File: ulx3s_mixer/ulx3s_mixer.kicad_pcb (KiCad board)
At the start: 4 copper layers, 66 x 62 mm, 47 parts, among them J1 Conn_02x20_Odd_Even, J2 Conn_Coaxial, Q1 BC846, U1 MAX2606, U2 ADEX-10L+, U3 VAM-6+, U4 PL133-27

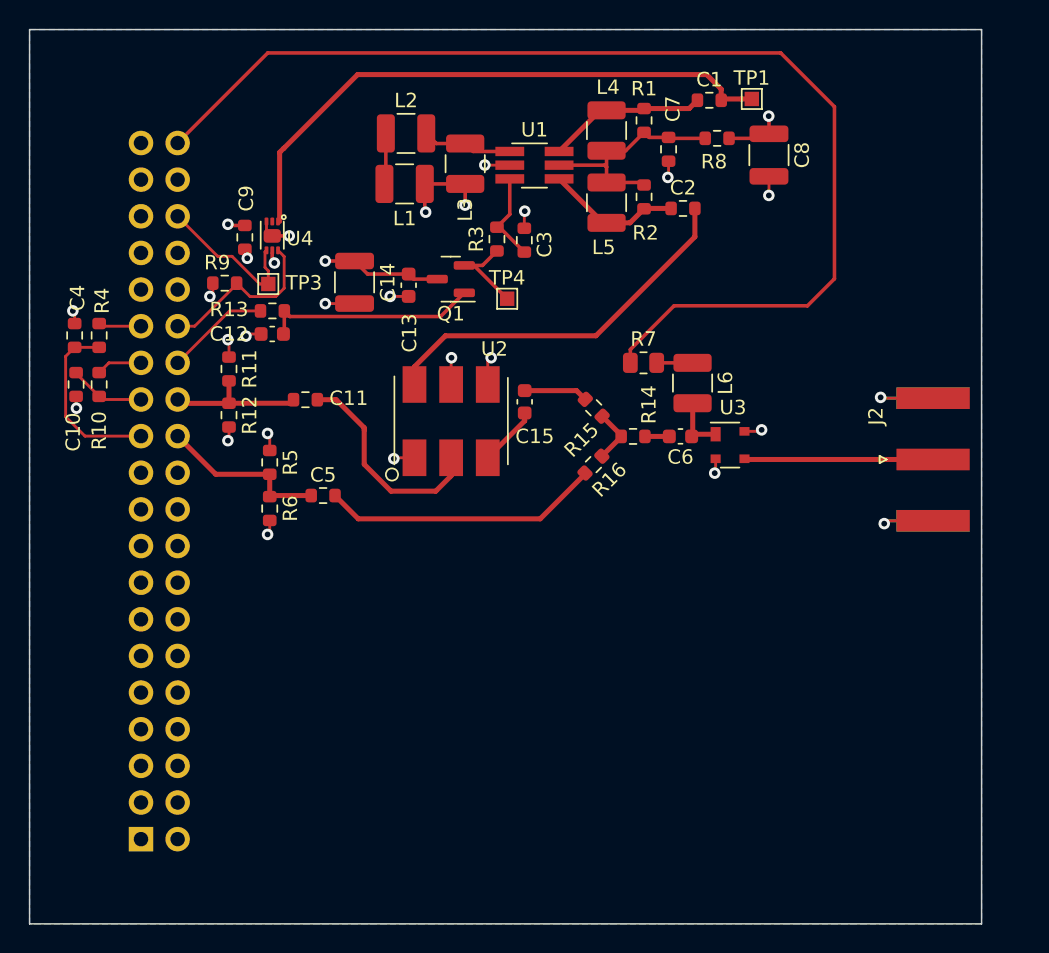
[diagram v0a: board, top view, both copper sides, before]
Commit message: Added design rules and poly pour (zone) on top layer
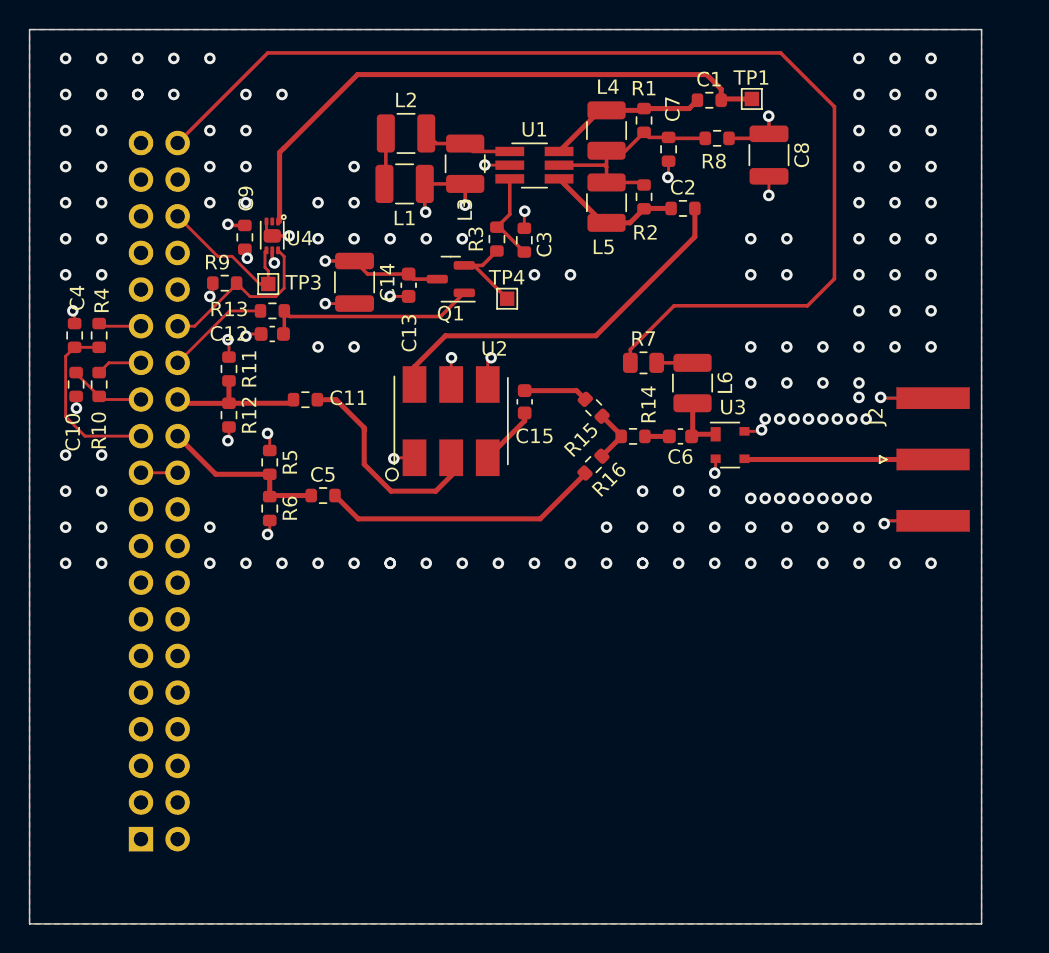
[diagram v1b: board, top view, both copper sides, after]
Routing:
- net GND: track 46.2 -> 48.7 mm, vias 23 -> 162
- added copper zone on F.Cu, net GND

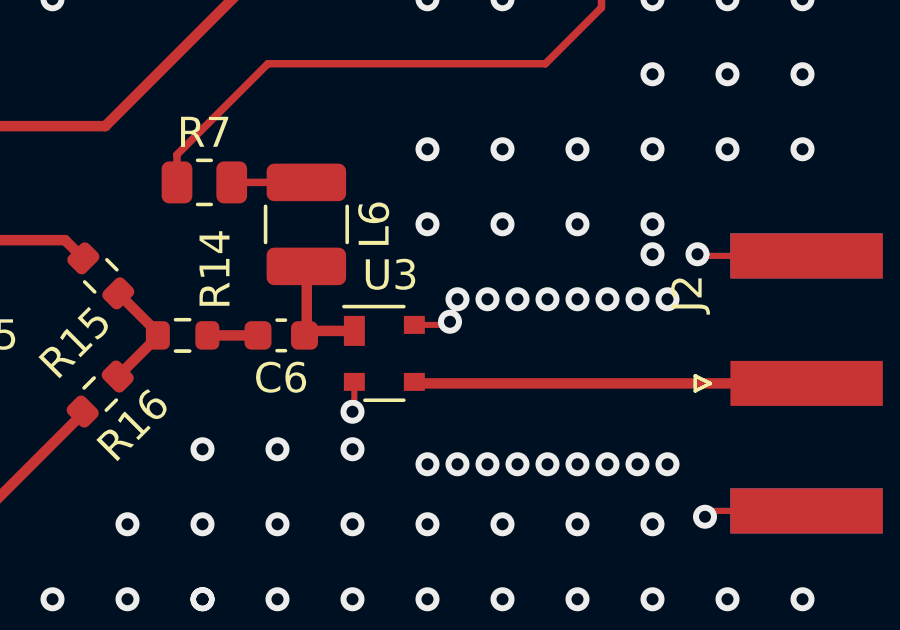
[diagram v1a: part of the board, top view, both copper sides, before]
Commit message: Added start of CS4344
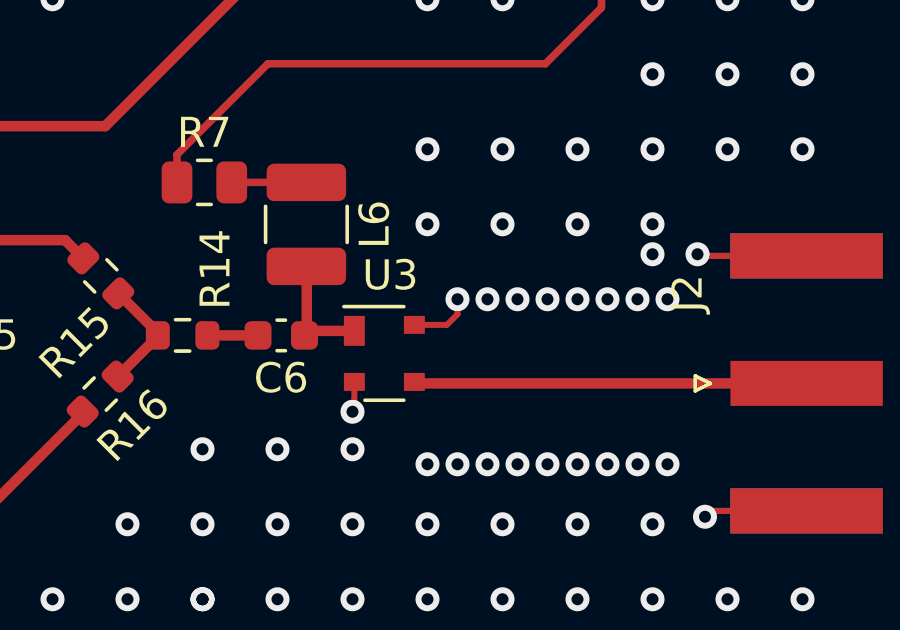
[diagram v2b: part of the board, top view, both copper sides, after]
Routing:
- net GND: track 48.7 -> 49.6 mm, vias 162 -> 161
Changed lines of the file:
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@@
   (segment (start 141.26 59.49) (end 141.25 59.5) (width 0.2) (layer "F.Cu") (net 6))
   (segment (start 116.685 77.685) (end 115.315 77.685) (width 0.2) (layer "F.Cu") (net 6))
-  (segment (start 140.645 75.855) (end 140.75 75.75) (width 0.2) (layer "F.Cu") (net 6))
-  (segment (start 139.5625 75.855) (end 140.645 75.855) (width 0.2) (layer "F.Cu") (net 6))
   (segment (start 134.3 57.125) (end 134.3 58.2) (width 0.2) (layer "F.Cu") (net 6))
   (segment (start 115.315 77.685) (end 115.25 77.75) (width 0.2) (layer "F.Cu") (net 6))
@@
   (segment (start 105.145 69.105) (end 105 69.25) (width 0.2) (layer "F.Cu") (net 6))
   (segment (start 137.5625 77.755) (end 137.5625 78.6875) (width 0.2) (layer "F.Cu") (net 6))
+  (segment (start 140.645 75.855) (end 141 75.5) (width 0.2) (layer "F.Cu") (net 6))
+  (segment (start 141 75.5) (end 141 75) (width 0.2) (layer "F.Cu") (net 6))
   (segment (start 116.28 66.5) (end 115 66.5) (width 0.2) (layer "F.Cu") (net 6))
   (segment (start 93.125 68.38) (end 93.125 67.625) (width 0.2) (layer "F.Cu") (net 6))
@@
   (segment (start 102.705 66.295) (end 102.5 66.5) (width 0.2) (layer "F.Cu") (net 6))
   (segment (start 149.055 73.555) (end 152.6375 73.555) (width 0.2) (layer "F.Cu") (net 6))
+  (segment (start 139.5625 75.855) (end 140.645 75.855) (width 0.2) (layer "F.Cu") (net 6))
   (segment (start 93.225 74.225) (end 93.25 74.25) (width 0.2) (layer "F.Cu") (net 6))
   (via (at 140 72.5) (size 0.8) (drill 0.4) (layers "F.Cu" "B.Cu") (free) (net 6))
@@
   (via (at 93 67.5) (size 0.8) (drill 0.4) (layers "F.Cu" "B.Cu") (net 6))
   (via (at 110 62.5) (size 0.8) (drill 0.4) (layers "F.Cu" "B.Cu") (free) (net 6))
-  (via (at 141 75) (size 0.8) (drill 0.4) (layers "F.Cu" "B.Cu") (free) (net 6))
   (via (at 137.5 80) (size 0.8) (drill 0.4) (layers "F.Cu" "B.Cu") (free) (net 6))
   (via (at 102.5 85) (size 0.8) (drill 0.4) (layers "F.Cu" "B.Cu") (free) (net 6))
@@
   (via (at 130 82.5) (size 0.8) (drill 0.4) (layers "F.Cu" "B.Cu") (free) (net 6))
   (via (at 127.5 65) (size 0.8) (drill 0.4) (layers "F.Cu" "B.Cu") (free) (net 6))
-  (via (at 147.5 82.5) (size 0.8) (drill 0.4) (layers "F.Cu" "B.Cu") (free) (net 6))
   (via (at 145 80.5) (size 0.8) (drill 0.4) (layers "F.Cu" "B.Cu") (free) (net 6))
   (via (at 117.5 62.5) (size 0.8) (drill 0.4) (layers "F.Cu" "B.Cu") (free) (net 6))
@@
   (via (at 110 85) (size 0.8) (drill 0.4) (layers "F.Cu" "B.Cu") (free) (net 6))
   (via (at 110 70) (size 0.8) (drill 0.4) (layers "F.Cu" "B.Cu") (free) (net 6))
-  (via (at 140.75 75.75) (size 0.8) (drill 0.4) (layers "F.Cu" "B.Cu") (net 6))
+  (via (at 141 75) (size 0.8) (drill 0.4) (layers "F.Cu" "B.Cu") (net 6))
   (via (at 122.5 85) (size 0.8) (drill 0.4) (layers "F.Cu" "B.Cu") (free) (net 6))
   (via (at 95 50) (size 0.8) (drill 0.4) (layers "F.Cu" "B.Cu") (free) (net 6))
@@
   (via (at 152.5 85) (size 0.8) (drill 0.4) (layers "F.Cu" "B.Cu") (free) (net 6))
   (via (at 135 80) (size 0.8) (drill 0.4) (layers "F.Cu" "B.Cu") (free) (net 6))
+  (via (at 147.5 82.5) (size 0.8) (drill 0.4) (layers "F.Cu" "B.Cu") (free) (net 6))
   (via (at 97.5 52.5) (size 0.8) (drill 0.4) (layers "F.Cu" "B.Cu") (free) (net 6))
   (via (at 132.5 85) (size 0.8) (drill 0.4) (layers "F.Cu" "B.Cu") (free) (net 6))

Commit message: Finished design, exported BOM + gerbers
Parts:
- added C16: 100nF, Capacitor_SMD:C_0603_1608Metric, F.Cu at (131.0, 96.0)
- added C17: 10uF, Capacitor_SMD:C_1210_3225Metric, F.Cu at (128.0, 94.5)
- added C18: 100nF, Capacitor_SMD:C_0603_1608Metric, F.Cu at (133.5, 94.3)
- added C19: 100nF, Capacitor_SMD:C_0603_1608Metric, F.Cu at (111.5, 95.3)
- added C20: 10uF, Capacitor_SMD:C_1210_3225Metric, F.Cu at (114.0, 95.5)
- added C21: 10uF, Capacitor_SMD:C_1210_3225Metric, F.Cu at (121.0, 97.0)
- added C22: 3.3uF, Capacitor_SMD:C_1210_3225Metric, F.Cu at (131.5, 103.0)
- added C23: 3.3uF, Capacitor_SMD:C_1210_3225Metric, F.Cu at (136.0, 95.0)
- added C24: 2.7nF, Capacitor_SMD:C_0603_1608Metric, F.Cu at (140.0, 96.0)
- added C25: 2.7nF, Capacitor_SMD:C_0603_1608Metric, F.Cu at (139.5, 104.0)
- added FB1: FerriteBead, Inductor_SMD:L_0402_1005Metric, F.Cu at (131.5, 93.5)
- added J3: AudioJack3_Ground, Connector_Audio:Jack_3.5mm_CUI_SJ-3523-SMT_Horizontal, F.Cu at (150.0, 98.5)
- added R17: 1R, Resistor_SMD:R_0603_1608Metric, F.Cu at (128.0, 98.5)
- added R18: 10k, Resistor_SMD:R_0603_1608Metric, F.Cu at (134.5, 103.0)
- added R19: 10k, Resistor_SMD:R_0603_1608Metric, F.Cu at (135.7, 90.5)
- added R20: 470R, Resistor_SMD:R_0603_1608Metric, F.Cu at (138.5, 101.5)
- added R21: 470R, Resistor_SMD:R_0603_1608Metric, F.Cu at (139.3, 93.5)
- added U5: CS4344, Package_SO:TSSOP-10_3x3mm_P0.5mm, F.Cu at (119.0, 92.5)
- R7: value 92R -> 100R
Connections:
- J1 pad 12: unconnected-(J1-Pad12) -> /MCLK
- J1 pad 14: unconnected-(J1-Pad14) -> /LRCLK
- J1 pad 16: unconnected-(J1-Pad16) -> /SCLK
- J1 pad 18: unconnected-(J1-Pad18) -> /SDIN
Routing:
- net +3V3: track 16.2 -> 56.0 mm
- net Net-(C22-Pad1): track 0.00 -> 23.9 mm
- net Net-(C23-Pad1): track 0.00 -> 21.5 mm
- net /SDIN: track 0.00 -> 19.8 mm
- net /SCLK: track 0.00 -> 18.9 mm
- net /LRCLK: track 0.00 -> 18.1 mm
- net /MCLK: track 0.00 -> 17.2 mm
- net Net-(C25-Pad2): track 0.00 -> 14.3 mm
- net +3.3VA: track 0.00 -> 12.2 mm
- net Net-(C22-Pad2): track 0.00 -> 6.72 mm
- net Net-(C24-Pad2): track 0.00 -> 6.16 mm
- net Net-(C19-Pad1): track 0.00 -> 5.76 mm
- net Net-(C23-Pad2): track 0.00 -> 5.04 mm
- net GND: track 49.6 -> 54.0 mm, vias 161 -> 273
- net Net-(C21-Pad1): track 0.00 -> 2.18 mm
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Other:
- board text added: "0"
- board text added: "0 mm"
- board text added: "0.01 mm"
- board text added: "0.0175 mm"
- board text added: "0.02"
- board text added: "0.035 mm"
- board text added: "0.196 mm"
- board text added: "1"
- board text added: "1.03 mm"
- board text added: "3.3"
- board text added: "4.5"
- board text added: "B.Cu"
- board text added: "B.Mask"
- board text added: "B.Paste"
- board text added: "B.Silkscreen"
- board text added: "Bottom Silk Screen"
- board text added: "Bottom Solder Mask"
- board text added: "Bottom Solder Paste"
- board text added: "Color"
- board text added: "Dielectric"
- board text added: "Epsilon R"
- board text added: "F.Cu"
- board text added: "F.Mask"
- board text added: "F.Paste"
- board text added: "F.Silkscreen"
- board text added: "FR4"
- board text added: "In1.Cu"
- board text added: "In2.Cu"
- board text added: "Layer Name"
- board text added: "Loss Tangent"
- board text added: "Material"
- board text added: "Not specified"
- board text added: "Thickness (mm)"
- board text added: "Top Silk Screen"
- board text added: "Top Solder Mask"
- board text added: "Top Solder Paste"
- board text added: "Type"
- board text added: "copper"
- board text added: "core"
- board text added: "prepreg"

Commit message: Rejigged soldermask clearance and regnereated fab outputs
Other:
- rule pad_to_mask_clearance: 0 -> 0.22
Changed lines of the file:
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@@
       (dielectric_constraints no)
     )
-    (pad_to_mask_clearance 0)
+    (pad_to_mask_clearance 0.22)
+    (solder_mask_min_width 0.22)
     (pcbplotparams
       (layerselection 0x00012fc_ffffffff)
@@
       (drillshape 0)
       (scaleselection 1)
-      (outputdirectory "outputs/pick_and_place/")
+      (outputdirectory "outputs/drill")
     )
   )
@@
     )
   )
-  (gr_arc (start 123.09 55.47) (mid 122.466216 54.492414) (end 123.097548 55.465142) (layer "F.SilkS") (width 0.15))
+  (gr_arc (start 123.09 55.47) (mid 122.466169 54.492444) (end 123.097548 55.465142) (layer "F.SilkS") (width 0.15))
   (gr_line (start 28.24 128.45) (end 28.24 185.66) (layer "Cmts.User") (width 0.1))
   (gr_line (start 28.24 177.53) (end 150.897143 177.53) (layer "Cmts.User") (width 0.1))
